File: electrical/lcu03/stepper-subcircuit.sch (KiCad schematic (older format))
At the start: 10 parts

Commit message: a
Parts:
- added R? (x2): 100 5%, symbol R
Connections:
- wire segments 51 -> 55
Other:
- note added: "These two through resistors \nbecause these two are switched \nvery often and to resuce a chance \nof false triggering because of digital \nnoise."
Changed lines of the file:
@@
 LIBS:lb1930mc
 LIBS:a4985
+LIBS:ts881
 LIBS:lcu03-cache
 EELAYER 25 0
@@
 Text HLabel 3600 3950 0    60   Input ~ 0
 ~sleep~
-Text HLabel 3600 4350 0    60   Input ~ 0
+Text HLabel 1000 4350 0    60   Input ~ 0
 step
 Text HLabel 3600 4550 0    60   Input ~ 0
 ref
-Text HLabel 5550 4350 2    60   Input ~ 0
+Text HLabel 1000 4600 0    60   Input ~ 0
 dir
 Text HLabel 5600 2550 2    60   Input ~ 0
@@
 Wire Wire Line
 	5600 2550 5250 2550
+$Comp
+L R R?
+U 1 1 566C867B
+P 1350 4350
+F 0 "R?" V 1430 4350 50  0000 C CNN
+F 1 "100 5%" V 1350 4350 50  0000 C CNN
+F 2 "" V 1280 4350 50  0000 C CNN
+F 3 "" H 1350 4350 50  0000 C CNN
+	1    1350 4350
+	0    1    1    0
+$EndComp
+Wire Wire Line
+	1500 4350 1800 4350
+Wire Wire Line
+	1200 4350 1000 4350
+Text Label 1600 4350 0    60   ~ 0
+step
+Text Label 3650 4350 0    60   ~ 0
+step
+$Comp
+L R R?
+U 1 1 566C8917
+P 1350 4600
+F 0 "R?" V 1430 4600 50  0000 C CNN
+F 1 "100 5%" V 1350 4600 50  0000 C CNN
+F 2 "" V 1280 4600 50  0000 C CNN
+F 3 "" H 1350 4600 50  0000 C CNN
+	1    1350 4600
+	0    1    1    0
+$EndComp
+Wire Wire Line
+	1500 4600 1800 4600
+Wire Wire Line
+	1200 4600 1000 4600
+Text Label 1600 4600 0    60   ~ 0
+dir
+Text Label 5350 4350 0    60   ~ 0
+dir
+Wire Notes Line
+	1300 4050 1200 3150
+Text Notes 700  3100 0    60   ~ 0
+These two through resistors \nbecause these two are switched \nvery often and to resuce a chance \nof false triggering because of digital \nnoise.
 $EndSCHEMATC

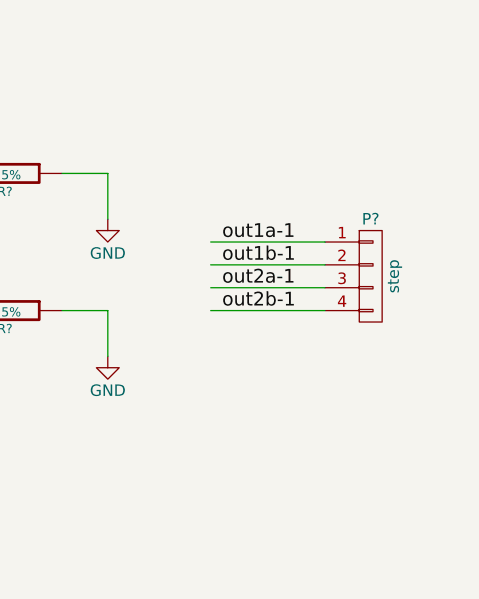
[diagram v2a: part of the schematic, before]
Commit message: Added specific socket used for stepper motors and for sensors.
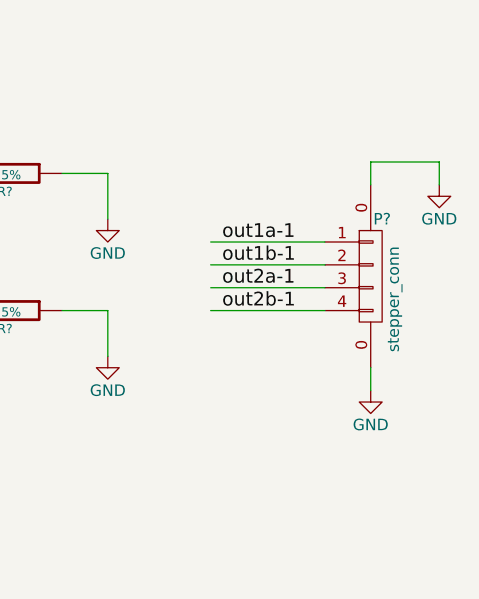
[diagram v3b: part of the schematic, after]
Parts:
- removed P?: step, symbol CONN_01X04
- added P?: stepper_conn, symbol stepper_conn
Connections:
- wire segments 55 -> 59
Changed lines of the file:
@@
 LIBS:ts881
 LIBS:m24c02
+LIBS:stepper_conn
 LIBS:lcu03-cache
 EELAYER 25 0
@@
 Text Label 5350 4150 0    60   ~ 0
 out1b-1
-$Comp
-L CONN_01X04 P?
-U 1 1 5667C73C
-P 10050 3600
-AR Path="/5667C1E7/5667C73C" Ref="P?"  Part="1"
-AR Path="/56687F5B/5667C73C" Ref="P?"  Part="1"
-F 0 "P?" H 10050 3850 50  0000 C CNN
-F 1 "step" V 10150 3600 50  0000 C CNN
-F 2 "" H 10050 3600 50  0000 C CNN
-F 3 "" H 10050 3600 50  0000 C CNN
-	1    10050 3600
-	1    0    0    -1
-$EndComp
 Text Label 9400 3650 0    60   ~ 0
 out2a-1
@@
 Text Notes 700  3100 0    60   ~ 0
 These two through resistors \nbecause these two are switched \nvery often and to resuce a chance \nof false triggering because of digital \nnoise.
+$Comp
+L stepper_conn P?
+U 1 1 5668FCA0
+P 10050 3600
+F 0 "P?" H 10100 3850 50  0000 C CNN
+F 1 "stepper_conn" V 10150 3500 50  0000 C CNN
+F 2 "" H 10050 3600 50  0000 C CNN
+F 3 "" H 10050 3600 50  0000 C CNN
+	1    10050 3600
+	1    0    0    -1
+$EndComp
+Wire Wire Line
+	10050 3200 10050 3100
+Wire Wire Line
+	10050 3100 10350 3100
+Wire Wire Line
+	10350 3100 10350 3200
+Wire Wire Line
+	10050 4000 10050 4100
+$Comp
+L GND #PWR?
+U 1 1 5668FCAB
+P 10050 4100
+F 0 "#PWR?" H 10050 3850 50  0001 C CNN
+F 1 "GND" H 10050 3950 50  0000 C CNN
+F 2 "" H 10050 4100 60  0000 C CNN
+F 3 "" H 10050 4100 60  0000 C CNN
+	1    10050 4100
+	1    0    0    -1
+$EndComp
+$Comp
+L GND #PWR?
+U 1 1 5668FCB1
+P 10350 3200
+F 0 "#PWR?" H 10350 2950 50  0001 C CNN
+F 1 "GND" H 10350 3050 50  0000 C CNN
+F 2 "" H 10350 3200 60  0000 C CNN
+F 3 "" H 10350 3200 60  0000 C CNN
+	1    10350 3200
+	1    0    0    -1
+$EndComp
 $EndSCHEMATC

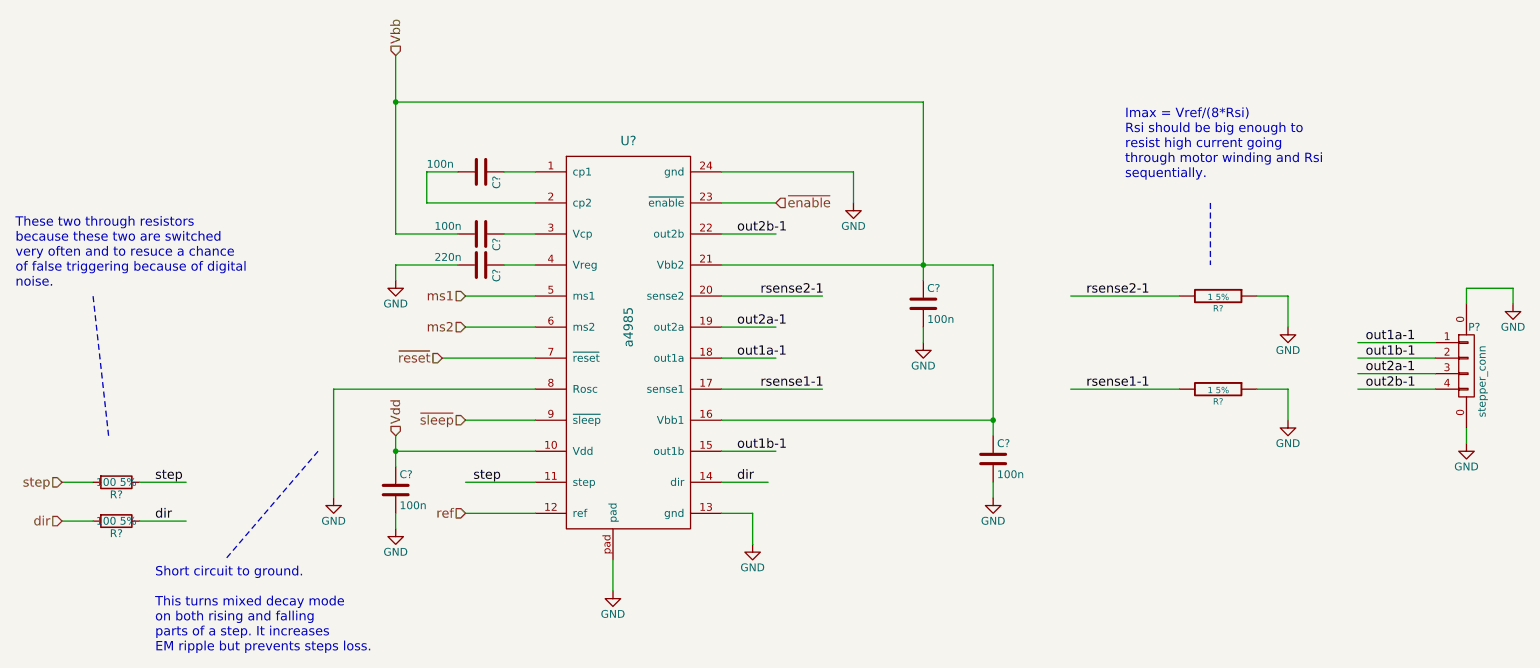
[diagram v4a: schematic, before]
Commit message: Added KiCad footprint libraries in file system as there are some troubles with access to them via github.com.
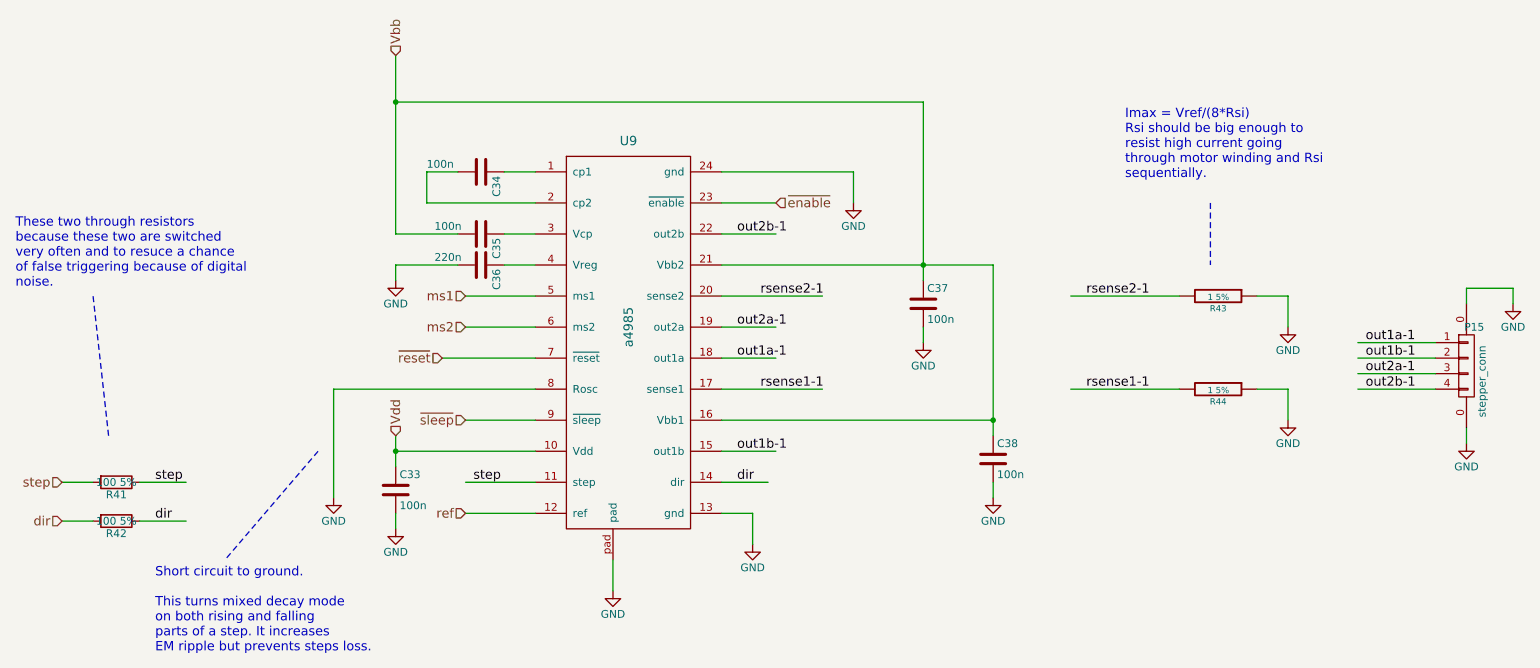
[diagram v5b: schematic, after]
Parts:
- gave numbers to parts that had none: 12

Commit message: a
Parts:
- C27, C28, C29, C30, C31, C32: footprint (none) -> Capacitors_SMD:C_0805
- P14: footprint (none) -> Connectors_JST_PH:Connectors_JST_B4B-PH-SM4-TB
- R37, R38: footprint (none) -> Resistors_SMD:R_0805
- R39, R40: footprint Resistors_SMD:R_0805_HandSoldering -> Resistors_SMD:R_0805
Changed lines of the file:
@@
 AR Path="/5667C1E7/5667C673" Ref="U8"  Part="1"
 AR Path="/56687F5B/5667C673" Ref="U9"  Part="1"
-F 0 "U9" H 4650 4550 60  0000 C CNN
+F 0 "U8" H 4650 4550 60  0000 C CNN
 F 1 "a4985" V 4650 3350 60  0000 C CNN
-F 2 "" H 4650 3350 60  0000 C CNN
+F 2 "" H 4650 3350 60  0001 C CNN
 F 3 "" H 4650 3350 60  0000 C CNN
 	1    4650 3350
@@
 AR Path="/5667C1E7/5667C682" Ref="C28"  Part="1"
 AR Path="/56687F5B/5667C682" Ref="C34"  Part="1"
-F 0 "C34" H 3725 2450 50  0000 L CNN
+F 0 "C28" H 3725 2450 50  0000 L CNN
 F 1 "100n" V 3650 2000 50  0000 L CNN
-F 2 "" H 3738 2200 50  0000 C CNN
+F 2 "Capacitors_SMD:C_0805" H 3738 2200 50  0001 C CNN
 F 3 "" H 3700 2350 50  0000 C CNN
 	1    3700 2350
@@
 AR Path="/5667C1E7/5667C68D" Ref="C29"  Part="1"
 AR Path="/56687F5B/5667C68D" Ref="C35"  Part="1"
-F 0 "C35" H 3725 2850 50  0000 L CNN
+F 0 "C29" H 3725 2850 50  0000 L CNN
 F 1 "100n" V 3650 2450 50  0000 L CNN
-F 2 "" H 3738 2600 50  0000 C CNN
+F 2 "Capacitors_SMD:C_0805" H 3738 2600 50  0001 C CNN
 F 3 "" H 3700 2750 50  0000 C CNN
 	1    3700 2750
@@
 AR Path="/5667C1E7/5667C697" Ref="C30"  Part="1"
 AR Path="/56687F5B/5667C697" Ref="C36"  Part="1"
-F 0 "C36" H 3725 3050 50  0000 L CNN
+F 0 "C30" H 3725 3050 50  0000 L CNN
 F 1 "220n" V 3650 2650 50  0000 L CNN
-F 2 "" H 3738 2800 50  0000 C CNN
+F 2 "Capacitors_SMD:C_0805" H 3738 2800 50  0001 C CNN
 F 3 "" H 3700 2950 50  0000 C CNN
 	1    3700 2950
@@
 AR Path="/5667C1E7/5667C6A1" Ref="#PWR095"  Part="1"
 AR Path="/56687F5B/5667C6A1" Ref="#PWR0107"  Part="1"
-F 0 "#PWR0107" H 3150 2800 50  0001 C CNN
+F 0 "#PWR095" H 3150 2800 50  0001 C CNN
 F 1 "GND" H 3150 2900 50  0000 C CNN
 F 2 "" H 3150 3050 50  0000 C CNN
@@
 AR Path="/5667C1E7/5667C6AF" Ref="C27"  Part="1"
 AR Path="/56687F5B/5667C6AF" Ref="C33"  Part="1"
-F 0 "C33" H 3175 4500 50  0000 L CNN
+F 0 "C27" H 3175 4500 50  0000 L CNN
 F 1 "100n" H 3175 4300 50  0000 L CNN
-F 2 "" H 3188 4250 50  0000 C CNN
+F 2 "Capacitors_SMD:C_0805" H 3188 4250 50  0001 C CNN
 F 3 "" H 3150 4400 50  0000 C CNN
 	1    3150 4400
@@
 AR Path="/5667C1E7/5667C6B8" Ref="#PWR096"  Part="1"
 AR Path="/56687F5B/5667C6B8" Ref="#PWR0108"  Part="1"
-F 0 "#PWR0108" H 3150 4400 50  0001 C CNN
+F 0 "#PWR096" H 3150 4400 50  0001 C CNN
 F 1 "GND" H 3150 4500 50  0000 C CNN
 F 2 "" H 3150 4650 50  0000 C CNN
@@
 AR Path="/5667C1E7/5667C6C4" Ref="#PWR097"  Part="1"
 AR Path="/56687F5B/5667C6C4" Ref="#PWR0109"  Part="1"
-F 0 "#PWR0109" H 5450 4500 50  0001 C CNN
+F 0 "#PWR097" H 5450 4500 50  0001 C CNN
 F 1 "GND" H 5450 4600 50  0000 C CNN
 F 2 "" H 5450 4750 50  0000 C CNN
@@
 AR Path="/5667C1E7/5667C6CB" Ref="#PWR098"  Part="1"
 AR Path="/56687F5B/5667C6CB" Ref="#PWR0110"  Part="1"
-F 0 "#PWR0110" H 4550 4800 50  0001 C CNN
+F 0 "#PWR098" H 4550 4800 50  0001 C CNN
 F 1 "GND" H 4550 4900 50  0000 C CNN
 F 2 "" H 4550 5050 50  0000 C CNN
@@
 AR Path="/5667C1E7/5667C6DE" Ref="#PWR099"  Part="1"
 AR Path="/56687F5B/5667C6DE" Ref="#PWR0111"  Part="1"
-F 0 "#PWR0111" H 2750 4200 50  0001 C CNN
+F 0 "#PWR099" H 2750 4200 50  0001 C CNN
 F 1 "GND" H 2750 4300 50  0000 C CNN
 F 2 "" H 2750 4450 50  0000 C CNN
@@
 AR Path="/5667C1E7/5667C6E6" Ref="#PWR0100"  Part="1"
 AR Path="/56687F5B/5667C6E6" Ref="#PWR0112"  Part="1"
-F 0 "#PWR0112" H 6550 3200 50  0001 C CNN
+F 0 "#PWR0100" H 6550 3200 50  0001 C CNN
 F 1 "GND" H 6550 3300 50  0000 C CNN
 F 2 "" H 6550 3450 50  0000 C CNN
@@
 AR Path="/5667C1E7/5667C6ED" Ref="#PWR0101"  Part="1"
 AR Path="/56687F5B/5667C6ED" Ref="#PWR0113"  Part="1"
-F 0 "#PWR0113" H 7000 4200 50  0001 C CNN
+F 0 "#PWR0101" H 7000 4200 50  0001 C CNN
 F 1 "GND" H 7000 4300 50  0000 C CNN
 F 2 "" H 7000 4450 50  0000 C CNN
@@
 AR Path="/5667C1E7/5667C6F4" Ref="R39"  Part="1"
 AR Path="/56687F5B/5667C6F4" Ref="R43"  Part="1"
-F 0 "R43" V 8530 3150 40  0000 C CNN
+F 0 "R39" V 8530 3150 40  0000 C CNN
 F 1 "1 5%" V 8457 3151 40  0000 C CNN
-F 2 "Resistors_SMD:R_0805_HandSoldering" V 8380 3150 30  0001 C CNN
+F 2 "Resistors_SMD:R_0805" V 8380 3150 30  0001 C CNN
 F 3 "~" H 8450 3150 30  0000 C CNN
 	1    8450 3150
@@
 AR Path="/5667C1E7/5667C701" Ref="C31"  Part="1"
 AR Path="/56687F5B/5667C701" Ref="C37"  Part="1"
-F 0 "C37" H 6575 3300 50  0000 L CNN
+F 0 "C31" H 6575 3300 50  0000 L CNN
 F 1 "100n" H 6575 3100 50  0000 L CNN
-F 2 "" H 6588 3050 50  0000 C CNN
+F 2 "Capacitors_SMD:C_0805" H 6588 3050 50  0001 C CNN
 F 3 "" H 6550 3200 50  0000 C CNN
 	1    6550 3200
@@
 AR Path="/5667C1E7/5667C708" Ref="C32"  Part="1"
 AR Path="/56687F5B/5667C708" Ref="C38"  Part="1"
-F 0 "C38" H 7025 4300 50  0000 L CNN
+F 0 "C32" H 7025 4300 50  0000 L CNN
 F 1 "100n" H 7025 4100 50  0000 L CNN
-F 2 "" H 7038 4050 50  0000 C CNN
+F 2 "Capacitors_SMD:C_0805" H 7038 4050 50  0001 C CNN
 F 3 "" H 7000 4200 50  0000 C CNN
 	1    7000 4200
@@
 AR Path="/5667C1E7/5667C713" Ref="#PWR0102"  Part="1"
 AR Path="/56687F5B/5667C713" Ref="#PWR0114"  Part="1"
-F 0 "#PWR0114" H 8900 3100 50  0001 C CNN
+F 0 "#PWR0102" H 8900 3100 50  0001 C CNN
 F 1 "GND" H 8900 3200 50  0000 C CNN
 F 2 "" H 8900 3350 50  0000 C CNN
@@
 AR Path="/5667C1E7/5667C719" Ref="R40"  Part="1"
 AR Path="/56687F5B/5667C719" Ref="R44"  Part="1"
-F 0 "R44" V 8530 3750 40  0000 C CNN
+F 0 "R40" V 8530 3750 40  0000 C CNN
 F 1 "1 5%" V 8457 3751 40  0000 C CNN
-F 2 "Resistors_SMD:R_0805_HandSoldering" V 8380 3750 30  0001 C CNN
+F 2 "Resistors_SMD:R_0805" V 8380 3750 30  0001 C CNN
 F 3 "~" H 8450 3750 30  0000 C CNN
 	1    8450 3750
@@
 AR Path="/5667C1E7/5667C724" Ref="#PWR0103"  Part="1"
 AR Path="/56687F5B/5667C724" Ref="#PWR0115"  Part="1"
-F 0 "#PWR0115" H 8900 3700 50  0001 C CNN
+F 0 "#PWR0103" H 8900 3700 50  0001 C CNN
 F 1 "GND" H 8900 3800 50  0000 C CNN
 F 2 "" H 8900 3950 50  0000 C CNN
@@
 AR Path="/5667C1E7/5667C72E" Ref="#PWR0104"  Part="1"
 AR Path="/56687F5B/5667C72E" Ref="#PWR0116"  Part="1"
-F 0 "#PWR0116" H 6100 2300 50  0001 C CNN
+F 0 "#PWR0104" H 6100 2300 50  0001 C CNN
 F 1 "GND" H 6100 2400 50  0000 C CNN
 F 2 "" H 6100 2550 50  0000 C CNN
@@
 AR Path="/5667C1E7/566C867B" Ref="R37"  Part="1"
 AR Path="/56687F5B/566C867B" Ref="R41"  Part="1"
-F 0 "R41" V 1430 4350 50  0000 C CNN
+F 0 "R37" V 1430 4350 50  0000 C CNN
 F 1 "100 5%" V 1350 4350 50  0000 C CNN
-F 2 "" V 1280 4350 50  0000 C CNN
+F 2 "Resistors_SMD:R_0805" V 1280 4350 50  0001 C CNN
 F 3 "" H 1350 4350 50  0000 C CNN
 	1    1350 4350
@@
 AR Path="/5667C1E7/566C8917" Ref="R38"  Part="1"
 AR Path="/56687F5B/566C8917" Ref="R42"  Part="1"
-F 0 "R42" V 1430 4600 50  0000 C CNN
+F 0 "R38" V 1430 4600 50  0000 C CNN
 F 1 "100 5%" V 1350 4600 50  0000 C CNN
-F 2 "" V 1280 4600 50  0000 C CNN
+F 2 "Resistors_SMD:R_0805" V 1280 4600 50  0001 C CNN
 F 3 "" H 1350 4600 50  0000 C CNN
 	1    1350 4600
@@
 AR Path="/5667C1E7/5668FCA0" Ref="P14"  Part="1"
 AR Path="/56687F5B/5668FCA0" Ref="P15"  Part="1"
-F 0 "P15" H 10100 3850 50  0000 C CNN
+F 0 "P14" H 10100 3850 50  0000 C CNN
 F 1 "stepper_conn" V 10150 3500 50  0000 C CNN
-F 2 "" H 10050 3600 50  0000 C CNN
+F 2 "Connectors_JST_PH:Connectors_JST_B4B-PH-SM4-TB" H 10050 3600 50  0001 C CNN
 F 3 "" H 10050 3600 50  0000 C CNN
 	1    10050 3600
@@
 AR Path="/5667C1E7/5668FCAB" Ref="#PWR0105"  Part="1"
 AR Path="/56687F5B/5668FCAB" Ref="#PWR0117"  Part="1"
-F 0 "#PWR0117" H 10050 3850 50  0001 C CNN
+F 0 "#PWR0105" H 10050 3850 50  0001 C CNN
 F 1 "GND" H 10050 3950 50  0000 C CNN
 F 2 "" H 10050 4100 60  0000 C CNN
@@
 AR Path="/5667C1E7/5668FCB1" Ref="#PWR0106"  Part="1"
 AR Path="/56687F5B/5668FCB1" Ref="#PWR0118"  Part="1"
-F 0 "#PWR0118" H 10350 2950 50  0001 C CNN
+F 0 "#PWR0106" H 10350 2950 50  0001 C CNN
 F 1 "GND" H 10350 3050 50  0000 C CNN
 F 2 "" H 10350 3200 60  0000 C CNN

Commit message: Looks like done with assigning footprints.
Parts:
- U8: footprint (none) -> my-lib:a4985
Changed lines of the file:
@@
 F 0 "U8" H 4650 4550 60  0000 C CNN
 F 1 "a4985" V 4650 3350 60  0000 C CNN
-F 2 "" H 4650 3350 60  0001 C CNN
+F 2 "my-lib:a4985" H 4650 3350 60  0001 C CNN
 F 3 "" H 4650 3350 60  0000 C CNN
 	1    4650 3350
